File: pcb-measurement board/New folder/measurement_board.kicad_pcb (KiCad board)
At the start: 4 copper layers, 60 x 45 mm, 92 parts, among them P1 HDR DUAL ROW, P2 CONN_02X15, P3 CONN_02X13, P4 CONN_02X05, P5 CONN_02X05, Q1 Si1101X, U1 NX3L4051, U10 TLV1G125, U11 NX3L4051, U12 MSP430G2955, U13 AD8603, U14 TLV1G125, U15 MCP4921, U16 AD8293, U17 NX3L4051, U18 NX3L4051, U19 QS4A110, U2 TPS73133, U20 QS4A110, U21 TLV1G125, U22 TLV1G125, U3 74CBTLV3253, U4 NX3L4051, U5 TPS73125, U6 AD8603, U7 MCP4921, U8 NX3L4051, U9 TLV1G125

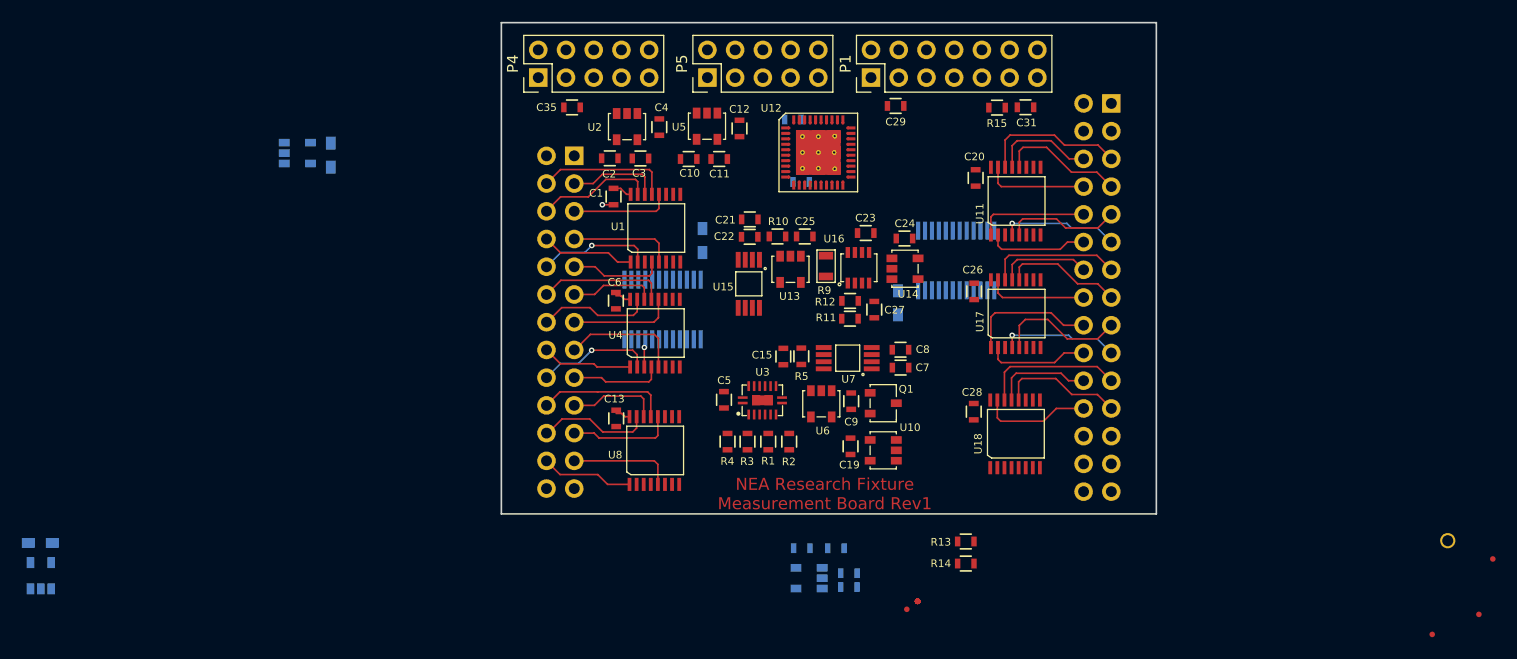
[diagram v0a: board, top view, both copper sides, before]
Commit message: -replaced all measurement board 0402 components with 0603 -adjusted placement and started routing on the layout
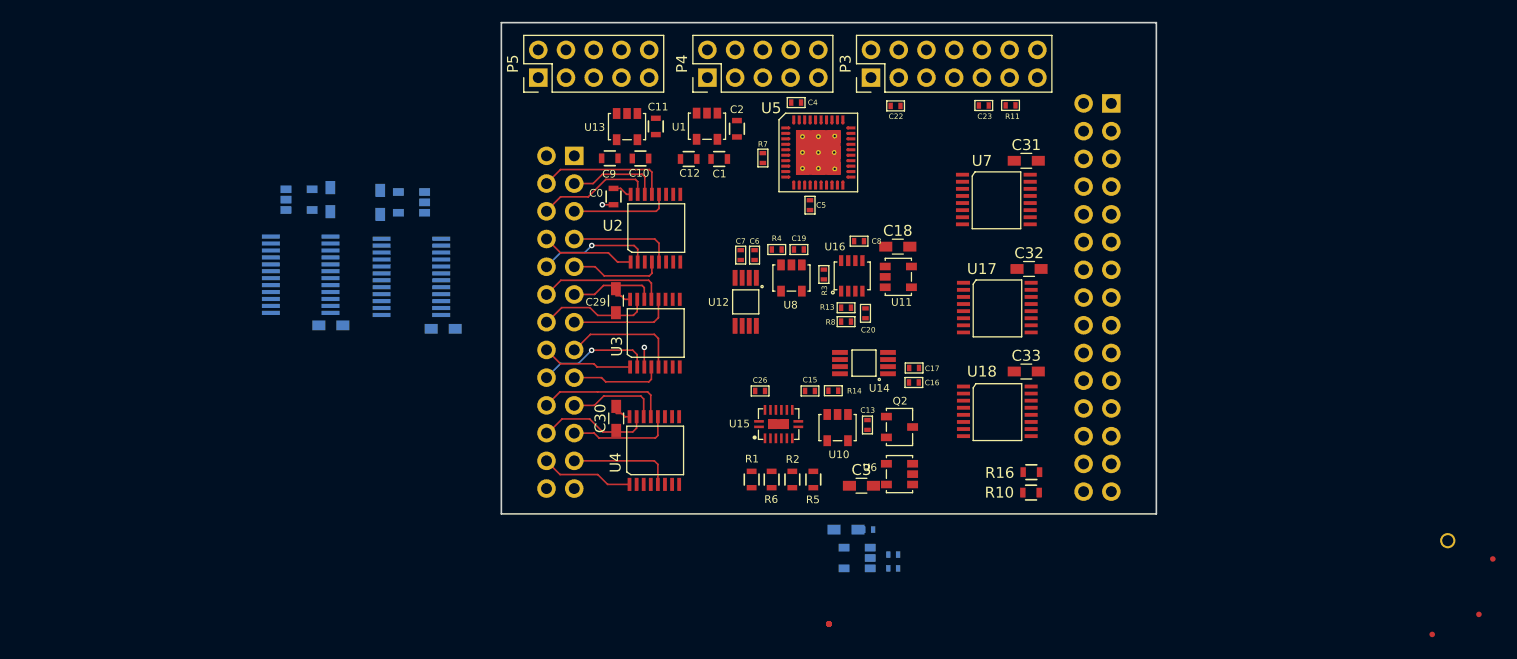
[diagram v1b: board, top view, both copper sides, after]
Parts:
- removed the C21 at (-7.24, -6.98)
- removed the C24 at (6.92, -5.23)
- removed the C25 at (-2.21, -5.41)
- removed C28: 0.1uF, footprints_on_Cdrive:0603
- removed C35: 10uF, footprints_on_Cdrive:0603
- removed the C9 at (2.05, 9.68)
- removed the R10 at (-4.71, -5.41)
- removed R15: 47K, footprints_on_Cdrive:0603
- removed the R5 at (-2.52, 5.56)
- removed the R6 at (1.84, 25.4)
- added C3: 0.1uF, Resistors_SMD:R_0603_HandSoldering, F.Cu at (2.99, 17.4)
- added C30: 0.1uF, Resistors_SMD:R_0603_HandSoldering, F.Cu at (-19.5, 11.3)
- added C32: 0.1uF, Resistors_SMD:R_0603_HandSoldering, F.Cu at (18.3, -2.44)
- added C33: 0.1uF, Resistors_SMD:R_0603_HandSoldering, F.Cu at (18.1, 6.96)
- added C4: 0.1uF, footprints_on_Cdrive:0402, F.Cu at (-3.00, -17.7)
- added R13: 18k, footprints_on_Cdrive:0402, F.Cu at (1.57, 1.12)
- added R14: 1K, footprints_on_Cdrive:0402, F.Cu at (0.41, 8.72)
- added R3: 10, footprints_on_Cdrive:0402, F.Cu at (-0.46, -1.93)
- added R4: 1K, footprints_on_Cdrive:0402, F.Cu at (-4.78, -4.22)
- added R8: 100k, footprints_on_Cdrive:0402, F.Cu at (1.57, 2.39)
- C13: value 0.1uF -> 51pF; footprint footprints_on_Cdrive:0603 -> footprints_on_Cdrive:0402
- C14: value 1.1nF -> 1nF; footprint footprints_on_Cdrive:0603 -> footprints_on_Cdrive:0402
- C15, C19, C26, C5, C8: footprint footprints_on_Cdrive:0603 -> footprints_on_Cdrive:0402
- C16: value 0.1uF -> 10uF; footprint footprints_on_Cdrive:0603 -> footprints_on_Cdrive:0402; moved to F.Cu
- C17: footprint footprints_on_Cdrive:0603 -> footprints_on_Cdrive:0402; moved to F.Cu
- C18: footprint footprints_on_Cdrive:0603 -> Resistors_SMD:R_0603_HandSoldering; moved to F.Cu
- C20: value 0.1uF -> 39nF; footprint footprints_on_Cdrive:0603 -> footprints_on_Cdrive:0402
- C22, C6: value 0.1uF -> 10uF; footprint footprints_on_Cdrive:0603 -> footprints_on_Cdrive:0402
- C23: value 0.1uF -> 1.1nF; footprint footprints_on_Cdrive:0603 -> footprints_on_Cdrive:0402
- C27: value 39nF -> 0.1uF; footprint footprints_on_Cdrive:0603 -> Resistors_SMD:R_0603_HandSoldering; moved to B.Cu
- C29: value 10uF -> 0.1uF; footprint footprints_on_Cdrive:0603 -> Resistors_SMD:R_0603_HandSoldering
- C31: value 1.1nF -> 0.1uF; footprint footprints_on_Cdrive:0603 -> Resistors_SMD:R_0603_HandSoldering
- C7: value 10uF -> 0.1uF; footprint footprints_on_Cdrive:0603 -> footprints_on_Cdrive:0402
- R11: value 100k -> 47K; footprint footprints_on_Cdrive:0603 -> footprints_on_Cdrive:0402
- R12: value 18k -> 100K; footprint footprints_on_Cdrive:0603 -> footprints_on_Cdrive:0402; moved to B.Cu
- R7: value 100k -> 47K; footprint footprints_on_Cdrive:0603 -> footprints_on_Cdrive:0402; moved to F.Cu
- R9: value 10ohm 0.1% -> 1K; footprint footprints_on_Cdrive:0805 -> footprints_on_Cdrive:0402; moved to B.Cu
- moved U22 49.9 mm to (-37.0, -8.53), turned to 90 degrees
- moved U20 49.7 mm to (-41.0, 1.78), turned to 90 degrees
- moved C34 44.1 mm to (-41.1, -8.53), turned to 90 degrees
- moved C24 41.7 mm to (-35.3, 3.05), turned to 180 degrees
- moved U19 39.4 mm to (-51.1, 1.58), turned to 90 degrees
- moved R7 36.4 mm to (-6.05, -12.6), turned to 90 degrees
- moved C21 34.9 mm to (-45.6, 2.73), turned to 180 degrees
- moved C29 31.2 mm to (-19.5, 0.47), turned to 90 degrees
- moved C18 29.0 mm to (6.31, -4.48), turned to 0 degrees
- moved R9 27.1 mm to (5.89, 23.7), turned to 180 degrees
- moved C16 26.5 mm to (7.79, 7.96)
- moved R11 24.5 mm to (16.6, -17.4), turned to 0 degrees
- moved C13 23.0 mm to (3.54, 11.9), turned to 270 degrees
- moved C26 21.6 mm to (-6.30, 8.74), turned to 180 degrees
- moved R12 21.0 mm to (3.61, 21.4)
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- renumbered C1 to C0, C11 to C1, C3 to C10, C4 to C11, C10 to C12, C12 to C2, C30 to C21, C32 to C24, C33 to C25, C2 to C9, P2 to P1, P3 to P2, P1 to P3, P5 to P4, P4 to P5, Q1 to Q2, R4 to R1, R14 to R10, R13 to R16, R1 to R2, R2 to R5, R3 to R6, TP11 to TP10, TP3 to TP11, TP4 to TP3, TP6 to TP4, TP7 to TP6, TP8 to TP7, TP9 to TP8, TP10 to TP9, U5 to U1, U6 to U10, U14 to U11, U15 to U12, U2 to U13, U7 to U14, U3 to U15, U1 to U2, U4 to U3, U8 to U4, U12 to U5, U10 to U6, U11 to U7, U13 to U8
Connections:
- C11 pad 1: /5V -> /VIN
- C13 pad 1: /3V3 -> /BIAS_OUT
- C13 pad 2: GND -> Net-(C13-Pad2)
- C19 pad 1: /3V3 -> Net-(C19-Pad1)
- C20 pad 1: /3V3 -> /Imeas
- C23 pad 1: Net-(C23-Pad1) -> /~RST
- C23 pad 2: Net-(C23-Pad2) -> GND
- C27 pad 1: /Imeas -> /3V3
- C31 pad 1: /~RST -> /3V3
- C8 pad 1: /3V3 -> Net-(C8-Pad1)
- C8 pad 2: GND -> Net-(C8-Pad2)
- Q2 pad 1: Net-(C9-Pad2) -> Net-(C13-Pad2)
- R11 pad 1: /0V5 -> /3V3
- R11 pad 2: /3V3 -> /~RST
- R12 pad 1: GND -> /~SELG
- R12 pad 2: /0V5 -> GND
- R7 pad 1: GND -> /~RST
- R7 pad 2: /~SELG -> /3V3
- R9 pad 2: Net-(R9-Pad2) -> Net-(C14-Pad1)
- TP4 pad 1: Net-(C25-Pad1) -> Net-(C19-Pad1)
- U10 pad 1: Net-(C9-Pad2) -> Net-(C13-Pad2)
- U11 pad 2: Net-(R9-Pad1) -> Net-(R3-Pad1)
- U13 pad 1: /5V -> /VIN
- U13 pad 3: /5V -> /VIN
- U16 pad 1: Net-(R9-Pad2) -> Net-(R3-Pad2)
- U16 pad 5: Net-(C23-Pad2) -> Net-(C8-Pad1)
- U16 pad 6: Net-(C23-Pad1) -> Net-(C8-Pad2)
- U16 pad 8: Net-(R9-Pad1) -> Net-(R3-Pad1)
- U8 pad 1: Net-(R9-Pad2) -> Net-(R3-Pad2)
- U8 pad 3: Net-(C25-Pad1) -> Net-(C19-Pad1)
- U8 pad 4: Net-(R9-Pad2) -> Net-(R3-Pad2)
- U9 pad 2: Net-(R6-Pad2) -> Net-(R9-Pad1)
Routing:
- net /M2: track 13.3 -> 0.00 mm
- net /U2: track 13.1 -> 0.00 mm
- net /Q2: track 12.3 -> 0.00 mm
- net /S2: track 11.9 -> 0.00 mm
- net /S1: track 11.9 -> 0.00 mm
- net /N2: track 11.5 -> 0.00 mm
- net /V2: track 11.4 -> 0.00 mm
- net /R2: track 11.0 -> 0.00 mm
- net /T2: track 10.9 -> 0.00 mm, vias 1 -> 0
- net /P2: track 10.9 -> 0.00 mm, vias 1 -> 0
- net /O2: track 10.6 -> 0.00 mm
- net /O1: track 10.2 -> 0.00 mm
- net /V1: track 10.1 -> 0.00 mm
- net /N1: track 9.44 -> 0.00 mm
- net /T1: track 9.42 -> 0.00 mm
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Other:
- board text removed: "NEA Research Fixture Measurement Board Rev1"
